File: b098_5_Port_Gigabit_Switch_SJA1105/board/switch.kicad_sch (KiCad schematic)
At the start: 28 parts, among them U1 SJA1105ELY

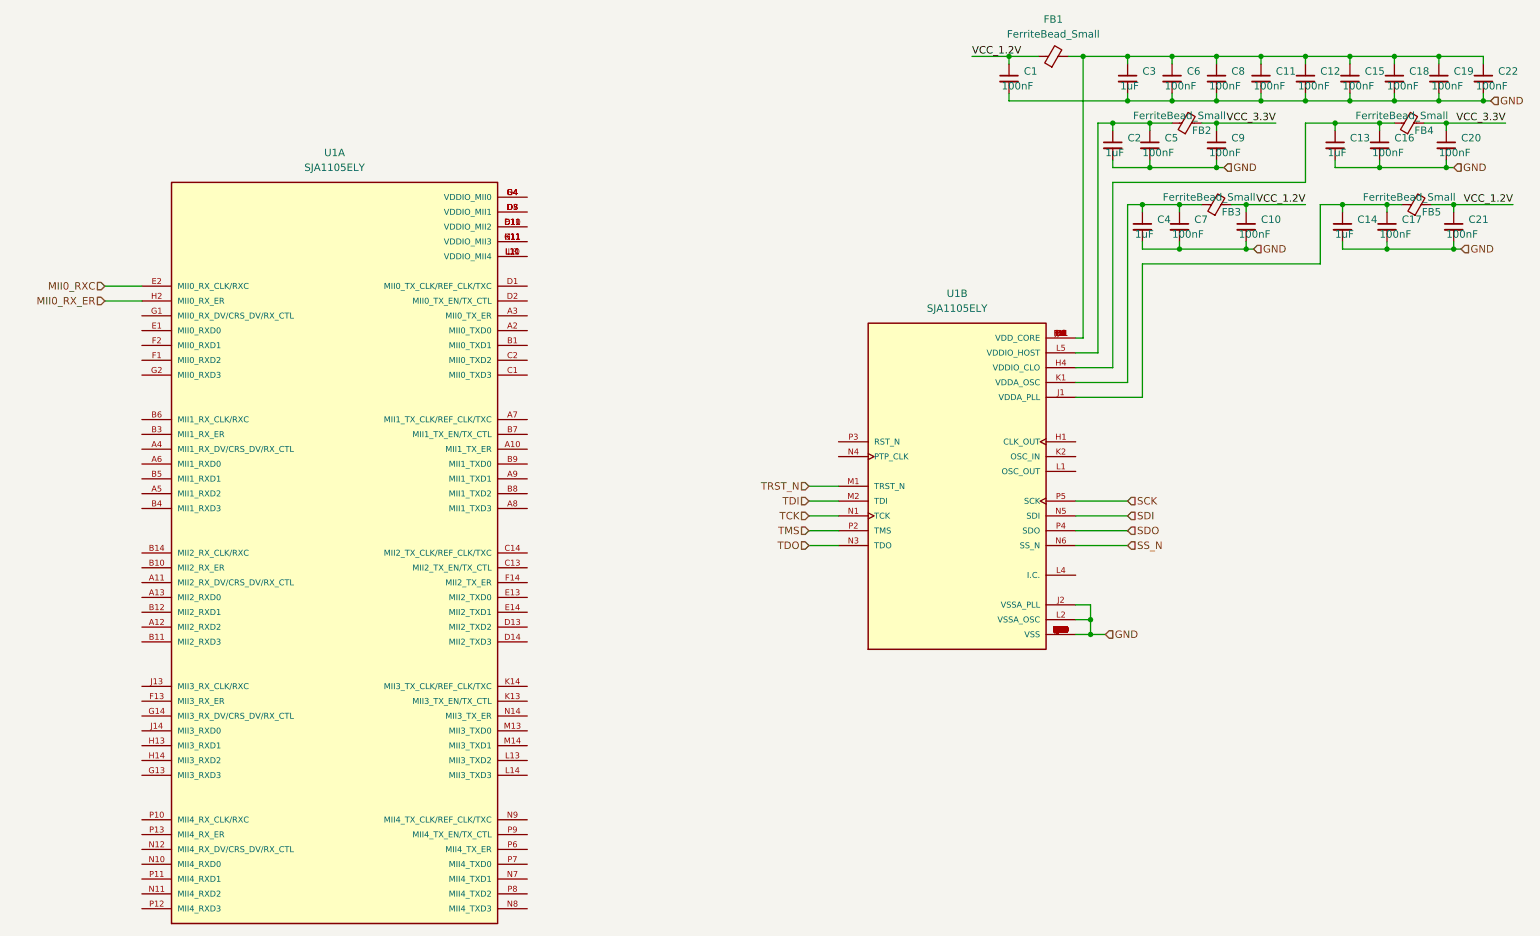
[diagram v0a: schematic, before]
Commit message: added the rest of the MII interfaces
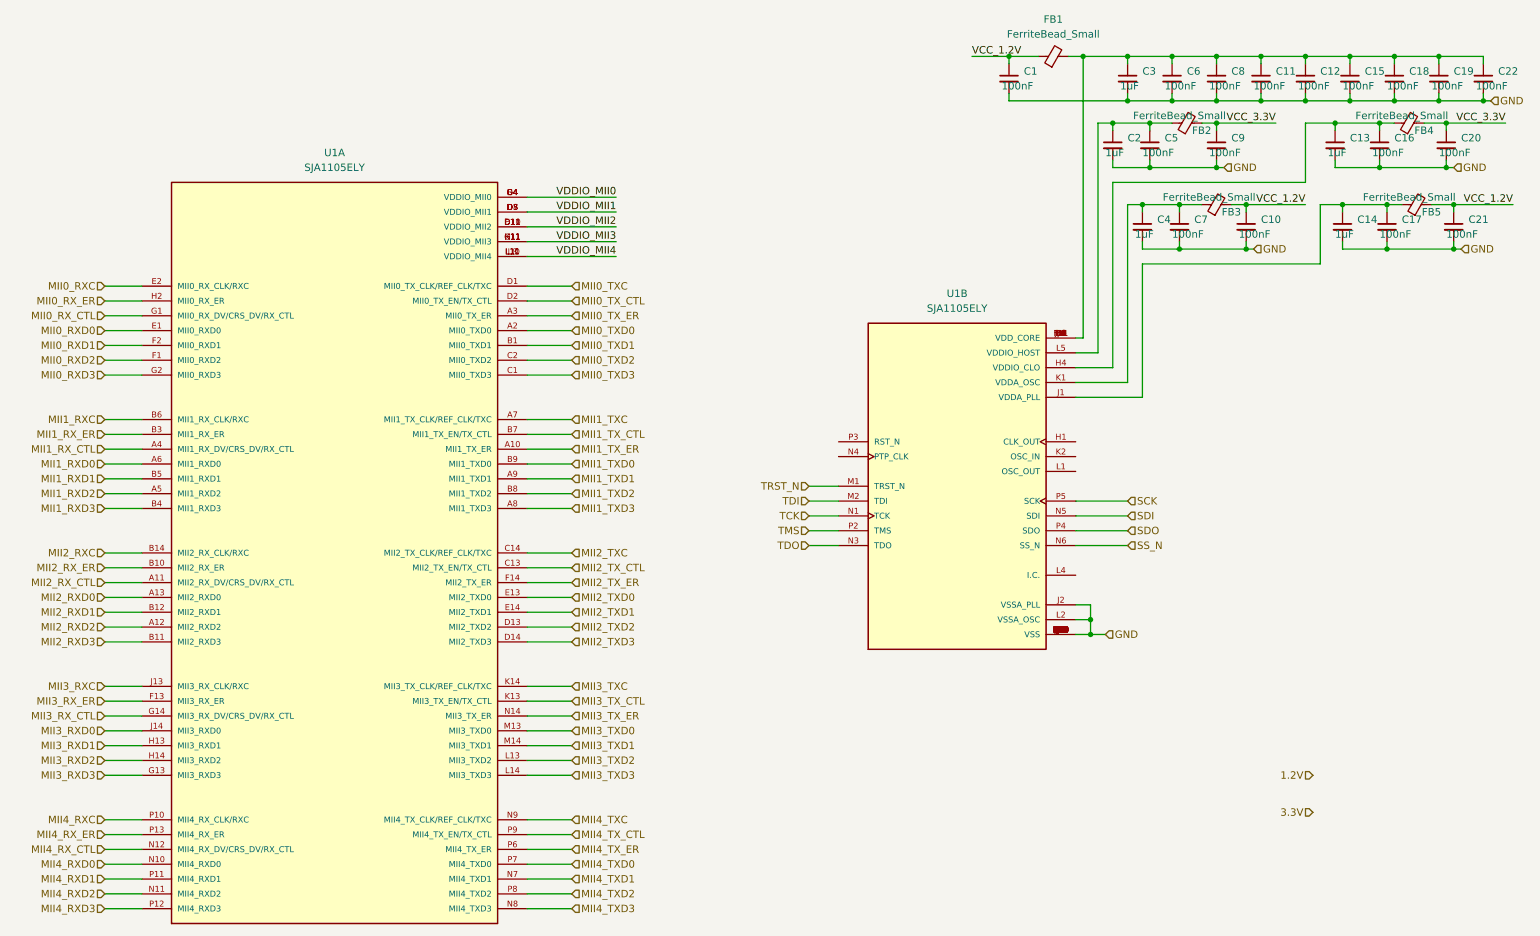
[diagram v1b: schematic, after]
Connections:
- net MII1_TX_ER: now reaches U1.A10 (MII1_TX_ER)
- net MII2_RX_CTL: now reaches U1.A11 (MII2_RX_DV/CRS_DV/RX_CTL)
- net MII2_RXD2: now reaches U1.A12 (MII2_RXD2)
- net MII2_RXD0: now reaches U1.A13 (MII2_RXD0)
- net MII0_TXD0: now reaches U1.A2 (MII0_TXD0)
- net MII0_TX_ER: now reaches U1.A3 (MII0_TX_ER)
- net MII1_RX_CTL: now reaches U1.A4 (MII1_RX_DV/CRS_DV/RX_CTL)
- net MII1_RXD2: now reaches U1.A5 (MII1_RXD2)
- net MII1_RXD0: now reaches U1.A6 (MII1_RXD0)
- net MII1_TXC: now reaches U1.A7 (MII1_TX_CLK/REF_CLK/TXC)
- net MII1_TXD3: now reaches U1.A8 (MII1_TXD3)
- net MII1_TXD1: now reaches U1.A9 (MII1_TXD1)
- net MII0_TXD1: now reaches U1.B1 (MII0_TXD1)
- net MII2_RX_ER: now reaches U1.B10 (MII2_RX_ER)
- net MII2_RXD3: now reaches U1.B11 (MII2_RXD3)
- net MII2_RXD1: now reaches U1.B12 (MII2_RXD1)
- net MII2_RXC: now reaches U1.B14 (MII2_RX_CLK/RXC)
- net MII1_RX_ER: now reaches U1.B3 (MII1_RX_ER)
- net MII1_RXD3: now reaches U1.B4 (MII1_RXD3)
- net MII1_RXD1: now reaches U1.B5 (MII1_RXD1)
- net MII1_RXC: now reaches U1.B6 (MII1_RX_CLK/RXC)
- net MII1_TX_CTL: now reaches U1.B7 (MII1_TX_EN/TX_CTL)
- net MII1_TXD2: now reaches U1.B8 (MII1_TXD2)
- net MII1_TXD0: now reaches U1.B9 (MII1_TXD0)
- net MII0_TXD3: now reaches U1.C1 (MII0_TXD3)
- net MII2_TX_CTL: now reaches U1.C13 (MII2_TX_EN/TX_CTL)
- net MII2_TXC: now reaches U1.C14 (MII2_TX_CLK/REF_CLK/TXC)
- net MII0_TXD2: now reaches U1.C2 (MII0_TXD2)
- net MII0_TXC: now reaches U1.D1 (MII0_TX_CLK/REF_CLK/TXC)
- net VDDIO_MII2: now reaches U1.D10 (VDDIO_MII2), U1.D11 (VDDIO_MII2), U1.E11 (VDDIO_MII2)
- net MII2_TXD2: now reaches U1.D13 (MII2_TXD2)
- net MII2_TXD3: now reaches U1.D14 (MII2_TXD3)
- net MII0_TX_CTL: now reaches U1.D2 (MII0_TX_EN/TX_CTL)
- net VDDIO_MII0: now reaches U1.D4 (VDDIO_MII0), U1.E4 (VDDIO_MII0), U1.G4 (VDDIO_MII0)
- net VDDIO_MII1: now reaches U1.D5 (VDDIO_MII1), U1.D7 (VDDIO_MII1), U1.D8 (VDDIO_MII1)
- net MII0_RXD0: now reaches U1.E1 (MII0_RXD0)
- net MII2_TXD0: now reaches U1.E13 (MII2_TXD0)
- net MII2_TXD1: now reaches U1.E14 (MII2_TXD1)
- net MII0_RXD2: now reaches U1.F1 (MII0_RXD2)
- net MII3_RX_ER: now reaches U1.F13 (MII3_RX_ER)
- net MII2_TX_ER: now reaches U1.F14 (MII2_TX_ER)
- net MII0_RXD1: now reaches U1.F2 (MII0_RXD1)
- net MII0_RX_CTL: now reaches U1.G1 (MII0_RX_DV/CRS_DV/RX_CTL)
- net VDDIO_MII3: now reaches U1.G11 (VDDIO_MII3), U1.H11 (VDDIO_MII3), U1.K11 (VDDIO_MII3)
- net MII3_RXD3: now reaches U1.G13 (MII3_RXD3)
- net MII3_RX_CTL: now reaches U1.G14 (MII3_RX_DV/CRS_DV/RX_CTL)
- net MII0_RXD3: now reaches U1.G2 (MII0_RXD3)
- net MII3_RXD1: now reaches U1.H13 (MII3_RXD1)
- net MII3_RXD2: now reaches U1.H14 (MII3_RXD2)
- net MII3_RXC: now reaches U1.J13 (MII3_RX_CLK/RXC)
- net MII3_RXD0: now reaches U1.J14 (MII3_RXD0)
- net MII3_TX_CTL: now reaches U1.K13 (MII3_TX_EN/TX_CTL)
- net MII3_TXC: now reaches U1.K14 (MII3_TX_CLK/REF_CLK/TXC)
- net VDDIO_MII4: now reaches U1.L10 (VDDIO_MII4), U1.L11 (VDDIO_MII4), U1.L8 (VDDIO_MII4)
- net MII3_TXD2: now reaches U1.L13 (MII3_TXD2)
- net MII3_TXD3: now reaches U1.L14 (MII3_TXD3)
- net MII3_TXD0: now reaches U1.M13 (MII3_TXD0)
- net MII3_TXD1: now reaches U1.M14 (MII3_TXD1)
- net MII4_RXD0: now reaches U1.N10 (MII4_RXD0)
- net MII4_RXD2: now reaches U1.N11 (MII4_RXD2)
- net MII4_RX_CTL: now reaches U1.N12 (MII4_RX_DV/CRS_DV/RX_CTL)
- net MII3_TX_ER: now reaches U1.N14 (MII3_TX_ER)
- net MII4_TXD1: now reaches U1.N7 (MII4_TXD1)
- net MII4_TXD3: now reaches U1.N8 (MII4_TXD3)
- net MII4_TXC: now reaches U1.N9 (MII4_TX_CLK/REF_CLK/TXC)
- net MII4_RXC: now reaches U1.P10 (MII4_RX_CLK/RXC)
- net MII4_RXD1: now reaches U1.P11 (MII4_RXD1)
- net MII4_RXD3: now reaches U1.P12 (MII4_RXD3)
- net MII4_RX_ER: now reaches U1.P13 (MII4_RX_ER)
- net MII4_TX_ER: now reaches U1.P6 (MII4_TX_ER)
- net MII4_TXD0: now reaches U1.P7 (MII4_TXD0)
- net MII4_TXD2: now reaches U1.P8 (MII4_TXD2)
- net MII4_TX_CTL: now reaches U1.P9 (MII4_TX_EN/TX_CTL)
